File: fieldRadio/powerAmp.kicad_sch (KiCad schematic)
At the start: 36 parts, among them Q1 PBSS4360Z, Q2 QH8KE5, T1 1:1, U1 74LVC2G04, U2 74LVC2G34, U3 MIC5205-3.3YM5

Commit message: Building fieldradio schematic
in process of building field radio schematics
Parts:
- added C10: 33pF, Capacitor_SMD:C_0603_1608Metric_Pad1.08x0.95mm_HandSolder, symbol powerAmp_RevB-eagle-import:CAP0603-CAP
- added D1: 1N4148, Diode_THT:D_DO-35_SOD27_P7.62mm_Horizontal, symbol Diode:1N4148
- added L2: L_Ferrite, Inductor_THT:L_Toroid_Vertical_L10.0mm_W5.0mm_P5.08mm, symbol Device:L_Ferrite
- added R5: 603-RC0603FR-0733KL, Resistor_SMD:R_0603_1608Metric_Pad0.98x0.95mm_HandSolder, symbol powerAmp_RevB-eagle-import:RESISTOR0603-RES
- added U4: 74LVC1G08, Package_TO_SOT_SMD:SOT-23-5_HandSoldering, symbol 74xGxx:74LVC1G08
- Q2: value QH8KE5 -> DMN10H220LPDW; footprint SamacSys_Parts:QH8K51TR -> SamacSys_Parts:DMN10H220LPDW13
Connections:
- net GND: now also C10.2, R5.1, U4.3 (GND)
- net RFin: now also D1.2 (A)
- net VCC3.3: now also U4.5 (VCC)
- net keyIn: now also U4.1; no longer R3.1, R7.2
- net at C6.2, L1.1, L1.4: now also L2.2; no longer C1.2, Q1.3 (E)
- net VCC12 renamed VDD12
- new net: C1.2, L2.1, Q1.3 (E)
- new net: C10.1, D1.1 (K), R5.2, U4.2
- new net: R3.1, R7.2, U4.4
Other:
- moved on the sheet: C1, C14, C15, C17, C18, C19, C2, C3, C4, C5, C6, C7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

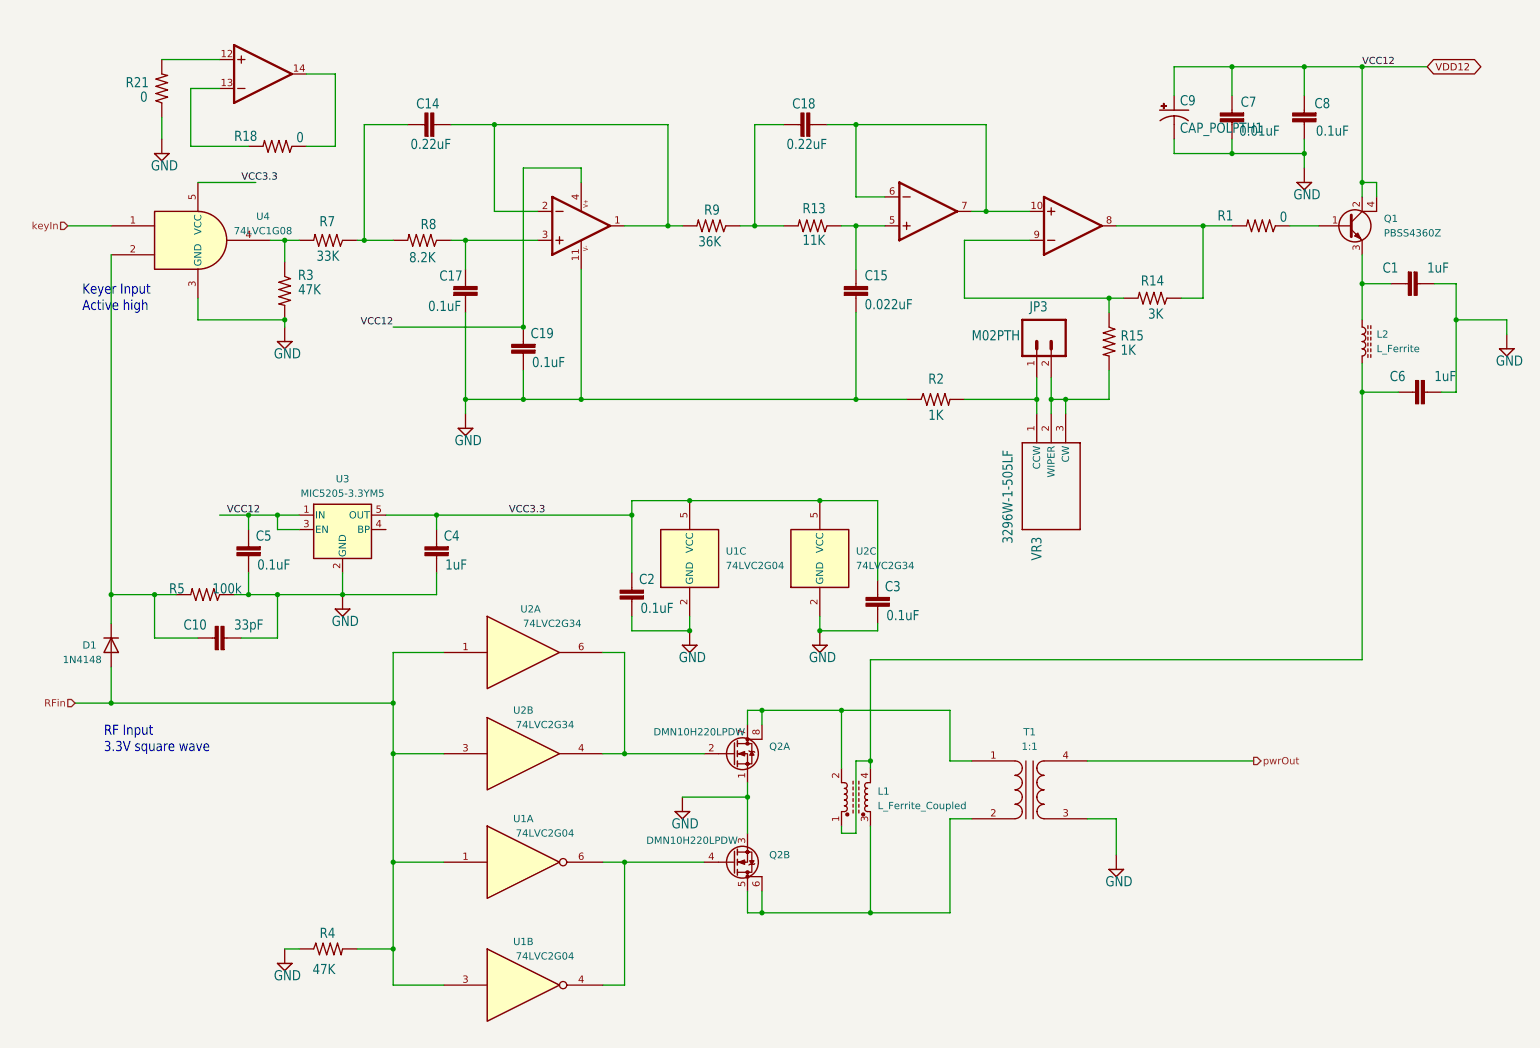
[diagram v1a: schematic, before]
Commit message: Updating field radio
Continued schematic work on field radio
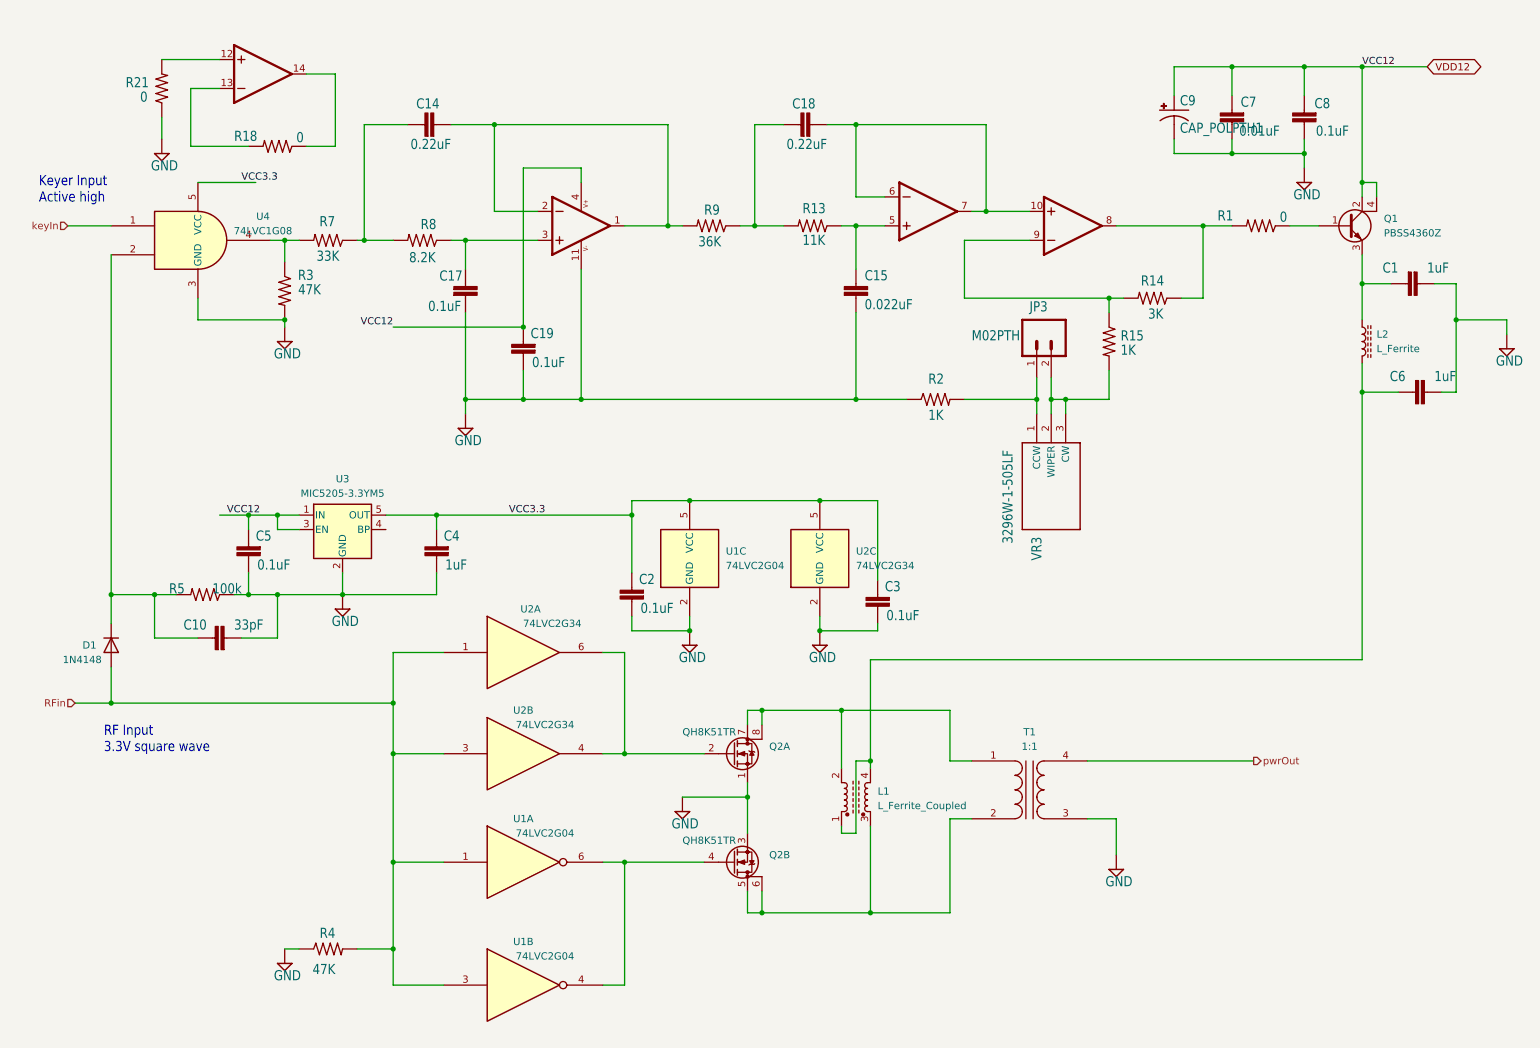
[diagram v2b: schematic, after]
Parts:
- Q2: value DMN10H220LPDW -> QH8K51TR; footprint SamacSys_Parts:DMN10H220LPDW13 -> SamacSys_Parts:QH8K51TR
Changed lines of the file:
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@@
     (effects (font (size 1.778 1.5113)) (justify left bottom))
   )
-  (text "Keyer Input\nActive high" (at 93.98 87.63 0)
+  (text "Keyer Input\nActive high" (at 86.36 68.58 0)
     (effects (font (size 1.778 1.5113)) (justify left bottom))
   )
@@
       (effects (font (size 1.27 1.27)) (justify left))
     )
-    (property "Value" "DMN10H220LPDW" (at 193.04 180.34 0)
+    (property "Value" "QH8K51TR" (at 199.39 180.34 0)
       (effects (font (size 1.27 1.27)) (justify left))
     )
-    (property "Footprint" "SamacSys_Parts:DMN10H220LPDW13" (at 213.36 184.15 0)
+    (property "Footprint" "SamacSys_Parts:QH8K51TR" (at 213.36 184.15 0)
       (effects (font (size 1.27 1.27)) hide)
     )
@@
       (effects (font (size 1.27 1.27)) (justify left))
     )
-    (property "Value" "DMN10H220LPDW" (at 194.31 161.29 0)
+    (property "Value" "QH8K51TR" (at 199.39 161.29 0)
       (effects (font (size 1.27 1.27)) (justify left))
     )
-    (property "Footprint" "SamacSys_Parts:DMN10H220LPDW13" (at 213.36 165.1 0)
-      (effects (font (size 1.27 1.27)) hide)
-    )
+    (property "Footprint" "SamacSys_Parts:QH8K51TR" (at 213.36 165.1 0)
+      (effects (font (size 1.27 1.27)) hide)
+    )

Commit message: More schematic dev.
More schematic development
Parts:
- removed R15: 603-RC0603FR-071KL, Resistor_SMD:R_0603_1608Metric_Pad0.98x0.95mm_HandSolder, symbol powerAmp_RevB-eagle-import:RESISTOR0603-RES
- added R38: 0, Resistor_SMD:R_0603_1608Metric_Pad0.98x0.95mm_HandSolder, symbol powerAmp_RevB-eagle-import:RESISTOR0603-RES
- added R40: DNP, Resistor_SMD:R_0603_1608Metric_Pad0.98x0.95mm_HandSolder, symbol powerAmp_RevB-eagle-import:RESISTOR0603-RES
- R39: renamed from R1; value 0 -> 10
- renumbered C10 to C37, C5 to C38, C14 to C39, C4 to C40, C17 to C41, C19 to C42, C2 to C43, C18 to C44, C15 to C45, C3 to C46, C9 to C47, C7 to C48, C8 to C49, C1 to C50, C6 to C51, D1 to D19, JP3 to JP1, L1 to L22, L2 to L23, Q2 to Q12, Q1 to Q13, R21 to R27, R5 to R28, R18 to R29, R3 to R30, R7 to R31, R4 to R32, R8 to R33, R9 to R34, R13 to R35, R2 to R36, R14 to R37, U$2 to U$1, U4 to U1, U3 to U2, U2 to U3, U1 to U4, VR3 to VR1
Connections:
- net at C50.2, L23.1, Q13.3 (E): now also R40.1
- net at JP1.2, VR1.2 (WIPER), VR1.3 (CW): now also R37.2, U$1.9 (-IN)
- net at R39.2, U$1.8 (OUT): now also R38.2; no longer R37.1
- new net: R37.1, R38.1, R40.2

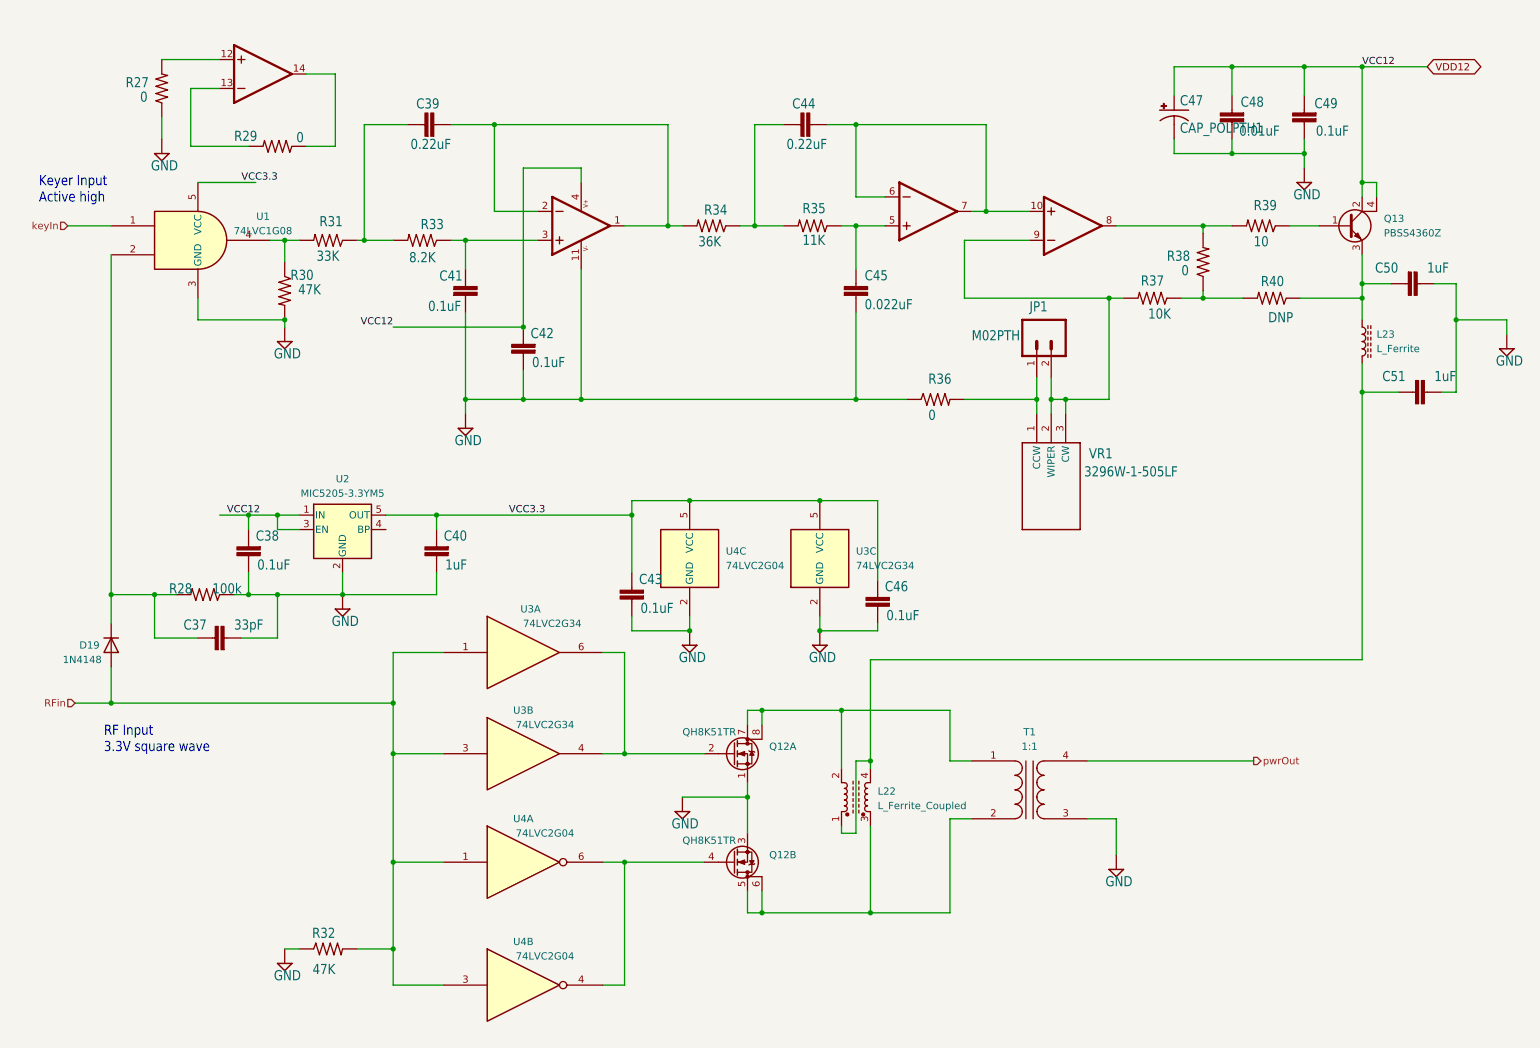
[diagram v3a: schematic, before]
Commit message: Update Connectors
Changed to PCB mount connectors for back panel
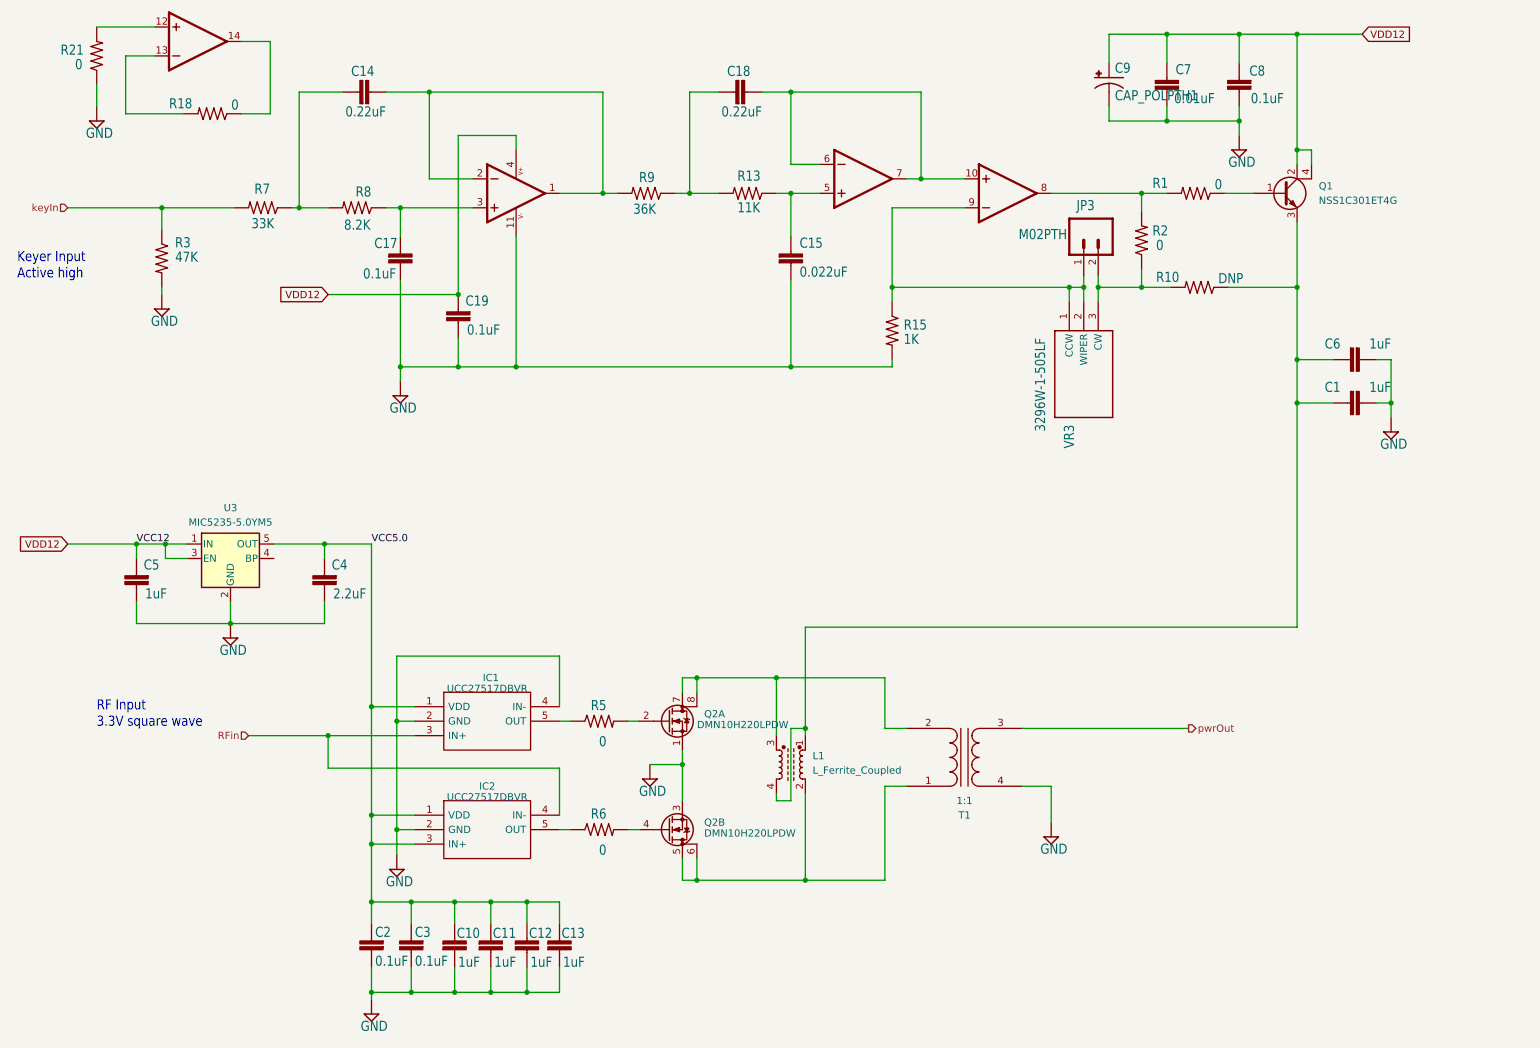
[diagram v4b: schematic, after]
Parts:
- removed C37: 33pF, Capacitor_SMD:C_0603_1608Metric_Pad1.08x0.95mm_HandSolder, symbol powerAmp_RevB-eagle-import:CAP0603-CAP
- removed D19: 1N4148, Diode_THT:D_DO-35_SOD27_P7.62mm_Horizontal, symbol Diode:1N4148
- removed L23: L_Ferrite, Inductor_THT:L_Toroid_Vertical_L10.0mm_W5.0mm_P5.08mm, symbol Device:L_Ferrite
- removed R28, R32: 603-RC0603FR-0733KL, Resistor_SMD:R_0603_1608Metric_Pad0.98x0.95mm_HandSolder, symbol powerAmp_RevB-eagle-import:RESISTOR0603-RES
- removed R36: 603-RC0603FR-071KL, Resistor_SMD:R_0603_1608Metric_Pad0.98x0.95mm_HandSolder, symbol powerAmp_RevB-eagle-import:RESISTOR0603-RES
- removed R37: 603-RC0603FR-073KL, Resistor_SMD:R_0603_1608Metric_Pad0.98x0.95mm_HandSolder, symbol powerAmp_RevB-eagle-import:RESISTOR0603-RES
- removed R38: 0, Resistor_SMD:R_0603_1608Metric_Pad0.98x0.95mm_HandSolder, symbol powerAmp_RevB-eagle-import:RESISTOR0603-RES
- removed R40: DNP, Resistor_SMD:R_0603_1608Metric_Pad0.98x0.95mm_HandSolder, symbol powerAmp_RevB-eagle-import:RESISTOR0603-RES
- removed U1: 74LVC1G08, Package_TO_SOT_SMD:SOT-23-5_HandSoldering, symbol 74xGxx:74LVC1G08
- removed U3: 74LVC2G34, Package_TO_SOT_SMD:SOT-23-6_Handsoldering, symbol 74xGxx:74LVC2G34
- removed U4: 74LVC2G04, Package_TO_SOT_SMD:SOT-23-6_Handsoldering, symbol 74xGxx:74LVC2G04
- added C10, C11, C12, C13: 1uF, Capacitor_SMD:C_0603_1608Metric_Pad1.08x0.95mm_HandSolder, symbol powerAmp_RevB-eagle-import:CAP0603-CAP
- added IC1, IC2: UCC27517DBVR, SOT95P280X145-5N, symbol SamacSys_Parts:UCC27517DBVR
- added R10: DNP, Resistor_SMD:R_0603_1608Metric_Pad0.98x0.95mm_HandSolder, symbol powerAmp_RevB-eagle-import:RESISTOR0603-RES
- added R15: 603-RC0603FR-071KL, Resistor_SMD:R_0603_1608Metric_Pad0.98x0.95mm_HandSolder, symbol powerAmp_RevB-eagle-import:RESISTOR0603-RES
- added R2: 0, Resistor_SMD:R_0603_1608Metric_Pad0.98x0.95mm_HandSolder, symbol powerAmp_RevB-eagle-import:RESISTOR0603-RES
- added R5, R6: 603-RC0603FR-0733KL, Resistor_SMD:R_0805_2012Metric_Pad1.20x1.40mm_HandSolder, symbol powerAmp_RevB-eagle-import:RESISTOR0603-RES
- C4: renamed from C40; value 1uF -> 2.2uF
- C5: renamed from C38; value 0.1uF -> 1uF
- L1: renamed from L22; footprint Transformer_THT:Transformer_Toroid_Horizontal_D14.0mm_Amidon-T50 -> SamacSys_Parts:Transformer_Balun_Amidon-T50
- Q1: renamed from Q13; value PBSS4360Z -> NSS1C301ET4G; footprint Package_TO_SOT_SMD:SOT-223 -> Package_TO_SOT_SMD:TO-252-3_TabPin4
- Q2: renamed from Q12; value QH8K51TR -> DMN10H220LPDW; footprint SamacSys_Parts:QH8K51TR -> SamacSys_Parts:DMN10H220LPDW13
- R1: renamed from R39; value 10 -> 0
- U3: renamed from U2; value MIC5205-3.3YM5 -> MIC5235-5.0YM5
- renumbered C50 to C1, C39 to C14, C45 to C15, C41 to C17, C44 to C18, C42 to C19, C43 to C2, C46 to C3, C51 to C6, C48 to C7, C49 to C8, C47 to C9, JP1 to JP3, R35 to R13, R29 to R18, R27 to R21, R30 to R3, R31 to R7, R33 to R8, R34 to R9, U$1 to U$2, VR1 to VR3
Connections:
- net GND: now also T1.4 (SB), C10.2, C11.2, C12.2, C13.2, IC1.2 (GND), IC1.4 (IN-), IC2.2 (GND), R15.2; no longer T1.3 (SA)
- net RFin: now also IC1.3 (IN+), IC2.4 (IN-)
- net keyIn: now also R3.1, R7.2
- net pwrOut: now also T1.3 (SA); no longer T1.4 (SB)
- net at C1.2, Q1.3 (E): now also C6.2, L1.1, L1.4, R10.1
- net at JP3.1, VR3.1 (CCW): now also U$2.9 (-IN), VR3.2 (WIPER), R15.1
- net at R1.2, U$2.8 (OUT): now also R2.2
- net at JP3.2, VR3.3 (CW): now also R10.2, R2.1; no longer U$2.9 (-IN), VR3.2 (WIPER)
- net at Q2.2 (G): now also R5.2
- net at L1.2, T1.1 (AA): now also Q2.5 (D), Q2.6 (D); no longer Q2.7 (D), Q2.8 (D)
- net at L1.3, T1.2 (AB): now also Q2.7 (D), Q2.8 (D); no longer Q2.5 (D), Q2.6 (D)
- net at Q2.4 (G): now also R6.2
- net VCC3.3 renamed VCC5.0
- net VCC5.0: now also C10.1, C11.1, C12.1, C13.1, IC1.1 (VDD), IC2.1 (VDD), IC2.3 (IN+)
- new net: IC1.5 (OUT), R5.1
- new net: IC2.5 (OUT), R6.1
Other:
- moved on the sheet: C1, C14, C15, C17, C18, C19, C2, C3, C4, C5, C6, C7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

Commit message: Clean Up
Schematic clean up in prep for layout
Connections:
- net GND: no longer C15.2, C17.2, C19.1, IC1.2 (GND), IC1.4 (IN-), IC2.2 (GND), R15.2, U$2.11 (V-)
- new net: IC1.2 (GND), IC1.4 (IN-), IC2.2 (GND)
- new net: C15.2, C17.2, C19.1, R15.2, U$2.11 (V-)
- no-connect marks 0 -> 1

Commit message: Placement Update
LPF and TR Switch placed
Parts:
- IC1, IC2: footprint SOT95P280X145-5N -> SamacSys_Parts:SOT95P280X145-5N
- L1: footprint SamacSys_Parts:Transformer_Balun_Amidon-T50 -> Transformer_THT:Autotransformer_Toroid_1Tap_Horizontal_D14.0mm_Amidon-T50
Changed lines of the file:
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@@
       (effects (font (size 1.27 1.27)))
     )
-    (property "Footprint" "SOT95P280X145-5N" (at 173.99 154.305 0)
+    (property "Footprint" "SamacSys_Parts:SOT95P280X145-5N" (at 173.99 154.305 0)
       (effects (font (size 1.27 1.27)) (justify left) hide)
     )
@@
       (effects (font (size 1.27 1.27)))
     )
-    (property "Footprint" "SOT95P280X145-5N" (at 173.99 173.355 0)
+    (property "Footprint" "SamacSys_Parts:SOT95P280X145-5N" (at 173.99 173.355 0)
       (effects (font (size 1.27 1.27)) (justify left) hide)
     )
@@
       (effects (font (size 1.27 1.27)) (justify left))
     )
-    (property "Footprint" "SamacSys_Parts:Transformer_Balun_Amidon-T50" (at 218.44 167.005 0)
-      (effects (font (size 1.27 1.27)) hide)
-    )
+    (property "Footprint" "Transformer_THT:Autotransformer_Toroid_1Tap_Horizontal_D14.0mm_Amidon-T50" (at 218.44 167.005 0)
+      (effects (font (size 1.27 1.27)) hide)
+    )
